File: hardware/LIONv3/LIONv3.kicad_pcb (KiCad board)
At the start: 4 copper layers, 51 x 86 mm, 97 parts, among them SW1 RESET, SW2 BOOT, U1 HC-1_25-2PWT, U10 E80-900M2213S, U11 W25Q16JVSSIQTR, U12 XL-1608UBC-04, U13 XL-1608UGC-04, U14 TPS259474ARPWR, U15 TLV76733DRVR, U16 XL-1608SURC-06, U17 INA226AIDGSR, U18 HC-1_25-2PWT, U19 HC-1_25-2PWT, U2 HC-1_25-2PWT, U20 HC-1_25-2PWT, U21 TCAN3414DR, U3 ESP32-C6-MINI-1-N4, U5 HC-1_25-2PWT, U6 TMP112AIDRLR, U7 USBLC6-2SC6, U8 TYPE-C_16PIN_2MD(073), U9 INA226AIDGSR

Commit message: refactor(hardware): improve via fencing
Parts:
- H1, H2, H3: footprint MountingHole:MountingHole_2.5mm_Pad -> MountingHole:MountingHole_2.5mm
- moved H2 45.3 mm to (71.3, 114.4)
- moved H3 44.5 mm to (116.0, 114.4)
- moved U20 1.61 mm to (110.2, 80.7)
- moved H1 0.92 mm to (116.0, 79.8)
- moved U3 0.22 mm to (82.7, 87.6)
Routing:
- net GND: track 0.00 -> 8.72 mm, vias 296 -> 326
- added copper zone on B.Cu, net GND
- added copper zone on In1.Cu, net GND
- added copper zone on In2.Cu, net GND
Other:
- board size 51 x 86 mm -> 50.2 x 85.2 mm

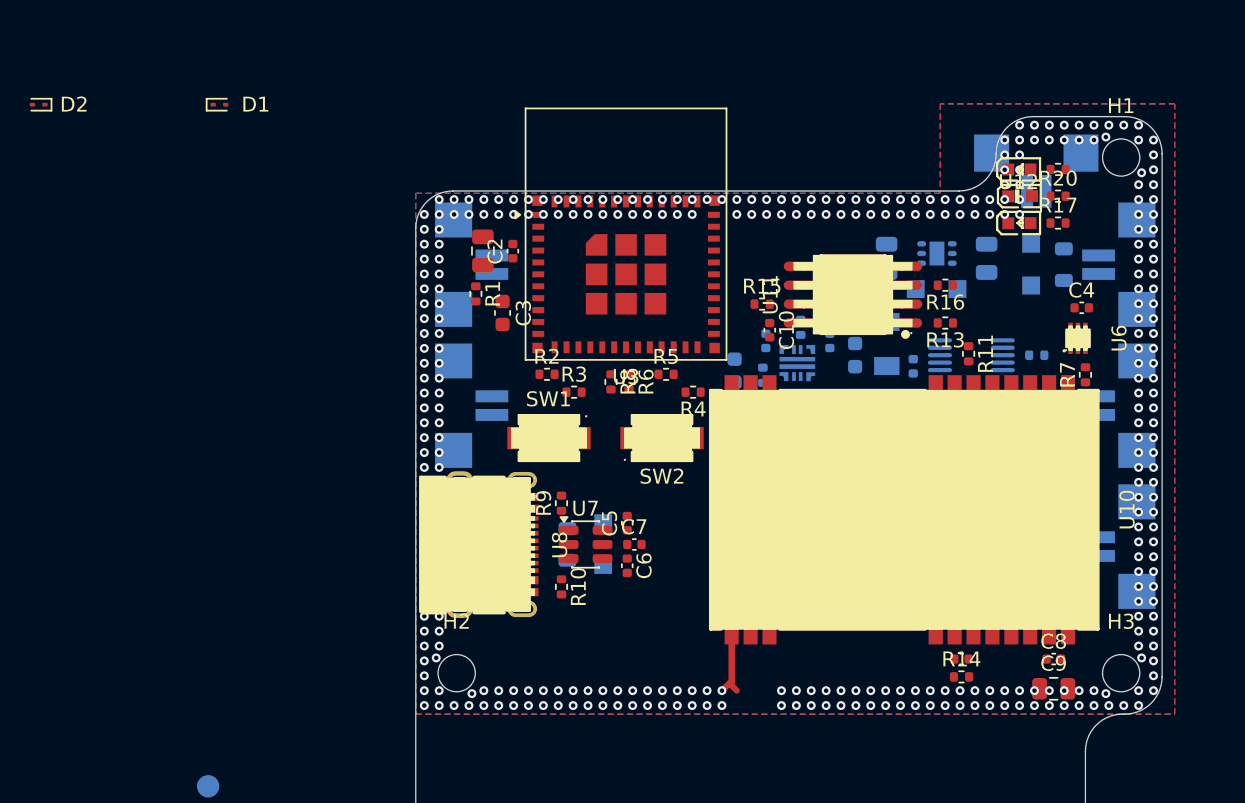
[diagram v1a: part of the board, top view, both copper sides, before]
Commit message: feat(hardware): add LED layout
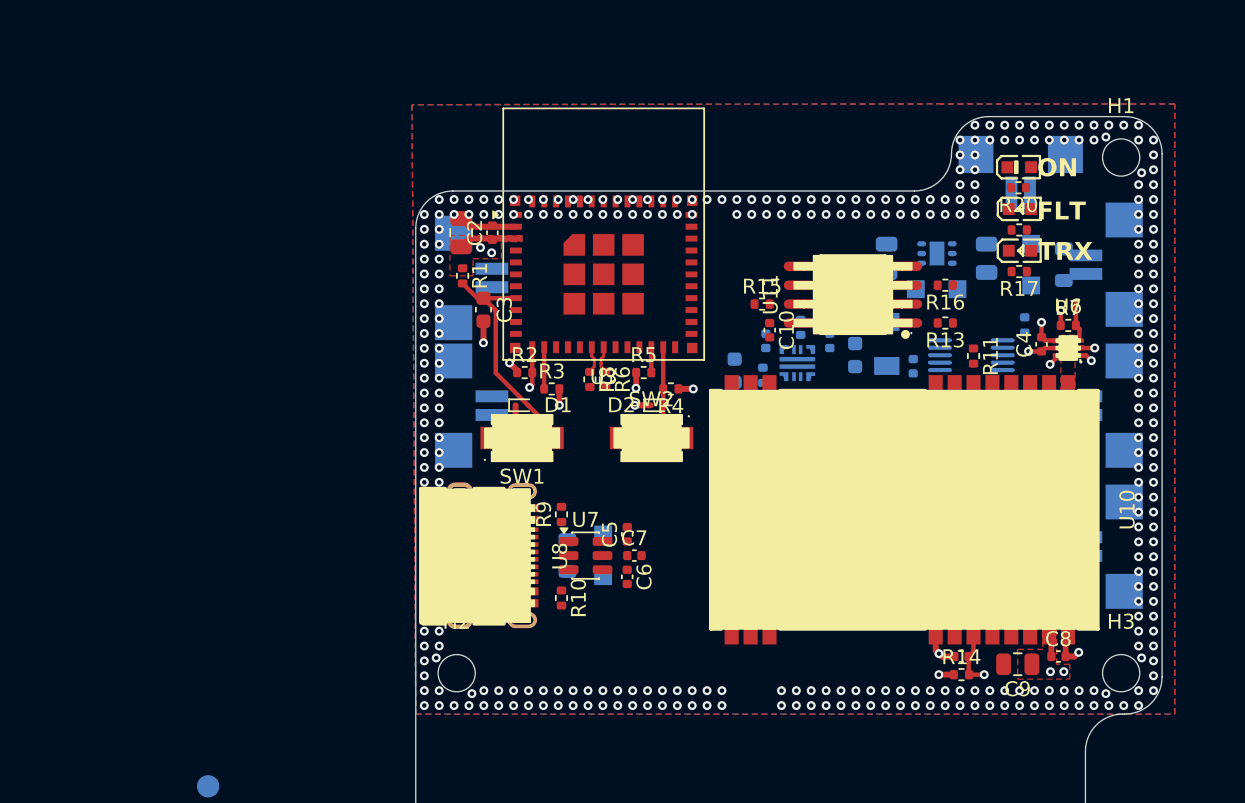
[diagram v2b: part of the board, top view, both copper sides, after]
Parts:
- moved D2 46.2 mm to (84.8, 96.4), turned to 0 degrees
- moved D1 28.7 mm to (75.7, 96.4)
- moved R24 4.83 mm to (109.1, 84.6), turned to 180 degrees
- moved R17 4.18 mm to (109.1, 87.4), turned to 180 degrees
- moved C4 3.65 mm to (110.6, 92.3), turned to 90 degrees
- moved R7 3.51 mm to (112.4, 91.0), turned to 0 degrees
- moved C9 2.93 mm to (109.0, 113.8), turned to 180 degrees
- moved R20 2.72 mm to (109.1, 81.8), turned to 180 degrees
- moved U16 2.65 mm to (109.2, 83.2)
- moved R27 2.19 mm to (109.5, 91.0), turned to 90 degrees
- moved U13 1.95 mm to (109.1, 80.4)
- moved C1 1.91 mm to (71.6, 84.8)
- moved U12 1.86 mm to (109.1, 86.0)
- moved C2 1.85 mm to (73.7, 84.8)
- moved SW1 1.80 mm to (75.7, 98.6), turned to 0 degrees
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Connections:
- net Net-(U3-IO12) renamed /ESP_USB_D-
- net Net-(U3-IO13) renamed /ESP_USB_D+
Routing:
- net Net-(D1-A2): track 0.00 -> 15.4 mm
- net +3.3V: track 0.00 -> 11.0 mm, vias 0 -> 8
- net GND: track 8.72 -> 19.6 mm, vias 326 -> 335
- net /IO9: track 0.00 -> 6.78 mm
- net /LR_RST: track 0.00 -> 4.25 mm, vias 0 -> 1
- net /I2C_SCL: track 0.00 -> 3.74 mm, vias 0 -> 1
- net /I2C_SDA: track 0.00 -> 3.57 mm, vias 0 -> 2
- net 3.3V_RF: track 0.00 -> 2.93 mm, vias 0 -> 3
- net /TMP_ALERT: track 0.00 -> 2.57 mm
- net /ESP_USB_D-: track 0.00 -> 1.85 mm
- net /ESP_USB_D+: track 0.00 -> 1.85 mm
- net /IO8: track 0.00 -> 1.70 mm
- added copper zone on F.Cu, net +3.3V
- added copper zone on F.Cu, net 3.3V_RF
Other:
- outline, holes or cut-outs redrawn
- board text added: "FLT"
- board text added: "ON"
- board text added: "TRX"

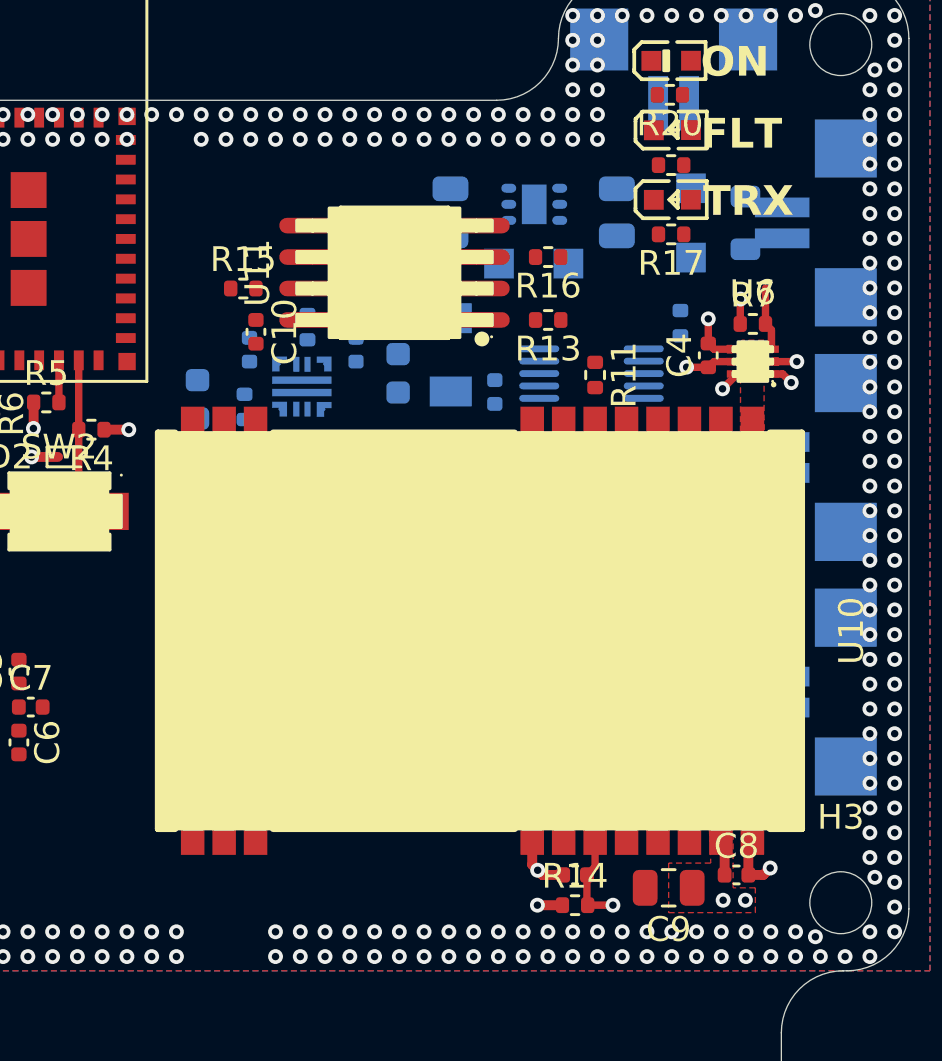
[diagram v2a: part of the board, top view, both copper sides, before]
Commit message: feat(hardware): start PDN design
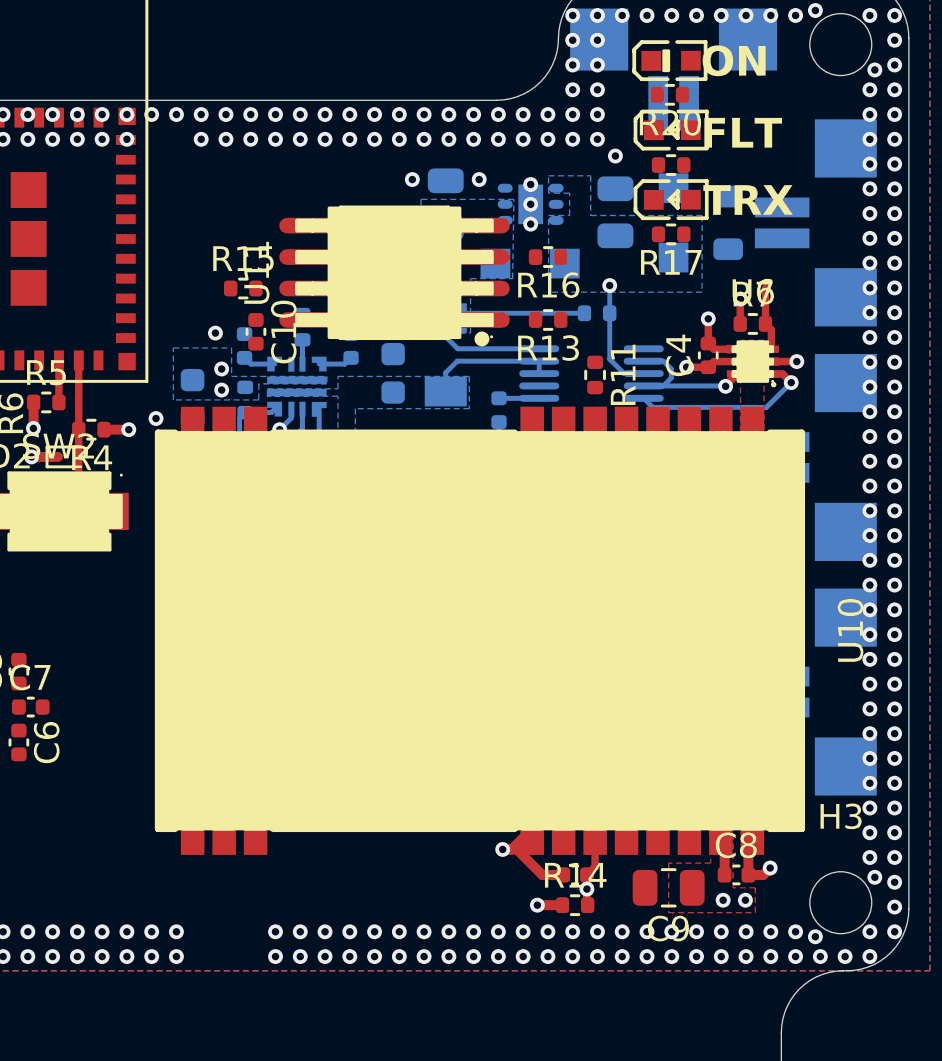
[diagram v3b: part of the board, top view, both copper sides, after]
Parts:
- moved R27 3.39 mm to (106.1, 90.6), turned to 180 degrees
- moved R12 0.88 mm to (99.2, 98.9)
- moved C19 0.75 mm to (102.2, 94.5), turned to -90 degrees
- moved D5 0.70 mm to (109.2, 87.0), turned to 90 degrees
- moved FB2 0.70 mm to (111.4, 87.0), turned to -90 degrees
- moved C16 0.37 mm to (100.0, 86.2)
- moved R19 0.28 mm to (91.9, 94.1)
- moved C17 0.25 mm to (96.2, 91.9)
- moved C18 0.25 mm to (91.9, 91.9)
- moved C14 0.20 mm to (97.9, 93.0)
- moved R21 0.20 mm to (94.9, 97.2)
- moved R22 0.20 mm to (91.7, 96.7)
- moved R26 0.20 mm to (100.0, 92.3)
- moved U14 0.20 mm to (94.0, 93.6)
- moved C13 0.20 mm to (89.8, 94.1)
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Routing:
- net +3.3V: track 11.0 -> 23.7 mm, vias 8 -> 11
- net +3.3V_LDO: track 0.00 -> 12.0 mm
- net GND: track 19.6 -> 30.4 mm, vias 335 -> 348
- net /I2C_SCL: track 3.74 -> 10.3 mm
- net /I2C_SDA: track 3.57 -> 9.58 mm
- net 3.3V_RF: track 2.93 -> 8.43 mm
- net +3.3V_eFuse: track 0.00 -> 5.22 mm
- net /INA_ALERT: track 0.00 -> 4.59 mm, vias 0 -> 1
- net Net-(U14-OVLO/OVCSEL): track 0.00 -> 3.56 mm
- net Net-(U14-EN/UVLO): track 0.00 -> 2.90 mm
- net Net-(U14-FLT#/PGTH): track 0.00 -> 2.89 mm
- net Net-(U14-ITIMER): track 0.00 -> 1.39 mm
- net Net-(U14-DVDT): track 0.00 -> 1.32 mm
- net /POWER/LED_FAULT: track 0.00 -> 1.02 mm, vias 0 -> 1
- net Net-(U14-ILM): track 0.00 -> 0.99 mm
- added copper zone on B.Cu, net +3.3V
- added copper zone on In2.Cu, net +3.3V
- added copper zone on B.Cu, net +3.3V_LDO
- added copper zone on B.Cu, net +3.3V_eFuse
- added copper zone on B.Cu, net +4.69V
- added copper zone on In2.Cu, net 3.3V_RF

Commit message: feat(hardware): improve PCB layout
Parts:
- C12, R11, R14, R15: moved to B.Cu
- C20, C21, C22, D6, JP1, R28, R29, TP1, TP2, TP3, TP4, TP5, TP6, TP7, TP8, TP9, U21: moved to F.Cu
- moved TP10 318.9 mm to (463.3, 86.7)
- moved TP12 318.9 mm to (463.3, 93.8)
- moved H2 295.2 mm to (365.9, 94.9)
- moved TP11 287.0 mm to (423.8, 93.5), turned to 180 degrees
- moved C13 259.0 mm to (348.7, 89.9)
- moved C11 258.1 mm to (359.6, 83.5)
- moved R12 257.6 mm to (356.5, 86.3), turned to 0 degrees
- moved R22 255.9 mm to (347.3, 86.1), turned to 90 degrees
- moved R15 255.7 mm to (346.4, 66.0)
- moved U20 255.6 mm to (364.8, 77.0), turned to -90 degrees
- moved R19 255.5 mm to (347.3, 88.2), turned to 90 degrees
- moved C18 255.4 mm to (347.3, 90.8), turned to -90 degrees
- moved C4 254.2 mm to (364.1, 73.7), turned to -90 degrees
- moved C10 253.7 mm to (344.7, 65.5), turned to 90 degrees
- moved R23 252.6 mm to (345.7, 86.1), turned to 90 degrees
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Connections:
- TP6 pad 1: /SPI_SCK -> /LR_LED
- U3 pad 15: /SPI_SCK -> /LR_LED
- U3 pad 16: /SPI_PICO -> /TMP_ALERT
- U3 pad 19: /LR_LED -> /CAN_RX
- U3 pad 20: /TMP_ALERT -> /CAN_TX
- U3 pad 24: /LR_CS# -> /CAN_STB
- U3 pad 26: /LR_BUSY -> /LR_IRQ
- U3 pad 27: /CAN_STB -> /LR_BUSY
- U3 pad 28: /CAN_TX -> /LR_CS#
- U3 pad 29: /CAN_RX -> /SPI_SCK
- U3 pad 30: /UART_RX -> /SPI_PICO
- U3 pad 31: /UART_TX -> /SPI_POCI
- U3 pad 5: /SPI_POCI -> /UART_RX
- U3 pad 6: /LR_IRQ -> /UART_TX
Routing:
- net /SPI_POCI: track 0.00 -> 34.7 mm, vias 0 -> 2
- net /LR_IRQ: track 0.00 -> 32.3 mm
- net /SPI_PICO: track 0.00 -> 29.6 mm, vias 0 -> 2
- net /SPI_SCK: track 0.00 -> 29.1 mm, vias 0 -> 2
- net /LR_RST: track 3.85 -> 30.8 mm, vias 1 -> 2
- net /LR_CS#: track 0.00 -> 23.4 mm, vias 0 -> 1
- net /LR_BUSY: track 0.00 -> 21.8 mm
- net +3.3V: track 23.7 -> 9.17 mm, vias 11 -> 24
- net /TMP_ALERT: track 2.57 -> 14.1 mm, vias 0 -> 1
- net GND: track 30.4 -> 18.9 mm, vias 348 -> 368
- net Net-(D1-A2): track 15.4 -> 7.49 mm
- net /I2C_SDA: track 9.58 -> 15.4 mm, vias 2 -> 1
- net +3.3V_LDO: track 12.0 -> 7.87 mm, vias 0 -> 2
- net /IO9: track 6.78 -> 3.84 mm
- net Net-(FB1-Pad2): track 0.00 -> 2.50 mm, vias 0 -> 2
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- added copper zone on B.Cu, net 3.3V_RF
- added copper zone on B.Cu, net Net-(D3-A)
- added copper zone on B.Cu, net Net-(FB1-Pad2)
- removed copper zone on F.Cu, net GND
- removed copper zone on In1.Cu, net GND
- removed copper zone on In2.Cu, net GND
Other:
- board size 50.2 x 85.2 mm -> 50.1 x 85.2 mm

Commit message: feat(hardware): finish PDN
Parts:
- removed C20: 10uF, Capacitor_SMD:C_0805_2012Metric
- removed C21: 100nF, Capacitor_SMD:C_0402_1005Metric
- removed C22: 4.7nF, Capacitor_SMD:C_0402_1005Metric
- removed D6: TI ESD752DBZR, Package_TO_SOT_SMD:SOT-23-3
- removed JP1: SolderJumper_3_Open, Jumper:SolderJumper-3_P2.0mm_Open_TrianglePad1.0x1.5mm
- removed R28, R29: 59, Resistor_SMD:R_0402_1005Metric
- removed TP1, TP10, TP11, TP12, TP2, TP3, TP4, TP5, TP6, TP7, TP8, TP9: TestPoint_Square, TestPoint:TestPoint_Pad_D1.5mm
- removed U21: TCAN3414DR, LIONv3-Footprints:SOIC-8_L4.9-W3.9-P1.27-LS6.0-BL
- R10, R9: moved to B.Cu
- moved U7 114.9 mm to (330.1, 86.8)
- moved U5 43.3 mm to (364.8, 68.2), turned to -90 degrees
- moved R5 41.1 mm to (333.2, 75.2), turned to 90 degrees
- moved U18 39.9 mm to (322.3, 76.6), turned to 90 degrees
- moved FB2 38.1 mm to (325.9, 77.6)
- moved C5 37.6 mm to (333.9, 88.2), turned to -90 degrees
- moved C7 36.7 mm to (334.3, 86.8)
- moved C6 36.4 mm to (333.9, 85.3), turned to 90 degrees
- moved R6 35.0 mm to (330.2, 75.2), turned to -90 degrees
- moved R3 34.3 mm to (326.7, 74.8)
- moved R8 33.9 mm to (329.2, 75.2), turned to -90 degrees
- moved D5 33.4 mm to (328.1, 79.5), turned to 90 degrees
- moved R2 32.3 mm to (324.7, 74.8)
- moved R10 29.6 mm to (323.5, 89.0), turned to 180 degrees
- moved R9 29.3 mm to (323.5, 86.0), turned to 180 degrees
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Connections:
- U7 pad 1: /D+ -> /D-
- U7 pad 3: /D- -> /D+
- U7 pad 4: /USB_D- -> /USB_D+
- U7 pad 6: /USB_D+ -> /USB_D-
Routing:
- net /INA_ALERT: track 3.71 -> 32.9 mm, vias 0 -> 3
- net /USB_D+: track 0.00 -> 27.3 mm
- net /USB_D-: track 0.00 -> 26.6 mm
- net /I2C_SCL: track 11.7 -> 25.8 mm, vias 1 -> 4
- net /I2C_SDA: track 15.4 -> 26.6 mm, vias 1 -> 2
- net GND: track 18.9 -> 10.1 mm, vias 368 -> 375
- net Net-(D1-A2): track 7.49 -> 14.0 mm
- net +3.3V: track 9.17 -> 14.2 mm, vias 24 -> 29
- net /IO9: track 3.84 -> 7.55 mm
- net /D-: track 0.00 -> 3.39 mm
- net /D+: track 0.00 -> 3.39 mm
- net +4.69V: track 0.00 -> 2.55 mm
- net /ESP_USB_D-: track 0.00 -> 1.90 mm
- net /ESP_USB_D+: track 0.00 -> 1.90 mm
- net Net-(U8-CC2): track 0.00 -> 1.89 mm, vias 0 -> 1
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- added copper zone on F.Cu, net GND
- added copper zone on In1.Cu, net GND
- added copper zone on In2.Cu, net GND
- added copper zone on B.Cu, net Net-(D5-A)
- added copper zone on B.Cu, net Net-(FB2-Pad2)
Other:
- board text added: "BOOT"
- board text added: "C6"
- board text added: "EN"
- board text added: "FLASH"
- board text added: "LIONv3-R"

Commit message: feat(hardware): route USB-C and CANbus differential pairs
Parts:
- added C20: 10uF, Capacitor_SMD:C_0805_2012Metric, F.Cu at (373.1, 53.8)
- added C21: 100nF, Capacitor_SMD:C_0402_1005Metric, F.Cu at (370.8, 65.2)
- added C22: 4.7nF, Capacitor_SMD:C_0402_1005Metric, F.Cu at (360.1, 60.7)
- added D6: TI ESD752DBZR, Package_TO_SOT_SMD:SOT-23-3, B.Cu at (360.1, 67.1)
- added JP1: SolderJumper_3_Open, Jumper:SolderJumper-3_P2.0mm_Open_TrianglePad1.0x1.5mm, F.Cu at (360.1, 63.0)
- added R28: 59, Resistor_SMD:R_0402_1005Metric, B.Cu at (361.2, 64.5)
- added R29: 59, Resistor_SMD:R_0402_1005Metric, B.Cu at (359.0, 64.5)
- added U21: TCAN3414DR, LIONv3-Footprints:SOIC-8_L4.9-W3.9-P1.27-LS6.0-BL, B.Cu at (354.3, 70.7)
- moved R17 15.8 mm to (375.7, 68.2)
- moved R20 15.8 mm to (375.7, 62.2)
- moved R24 15.8 mm to (375.7, 65.2)
- moved U13 15.8 mm to (375.4, 63.7)
- moved U12 15.8 mm to (375.5, 69.7)
- moved U16 15.8 mm to (375.5, 66.7)
- moved C7 7.37 mm to (329.7, 81.0), turned to 90 degrees
- moved C5 7.29 mm to (331.1, 81.5), turned to 0 degrees
- moved C6 6.82 mm to (328.3, 81.5), turned to 180 degrees
- moved U7 2.75 mm to (329.7, 84.1), turned to 90 degrees
- moved FB1 1.54 mm to (328.9, 87.3)
- moved D3 1.20 mm to (331.1, 87.0)
- moved U19 0.72 mm to (364.8, 76.3)
- moved C15 0.50 mm to (331.5, 91.3)
- moved U5 0.50 mm to (364.8, 67.7)
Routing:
- net /USB_D+: track 27.3 -> 7.63 mm
- net /USB_D-: track 26.6 -> 7.63 mm
- net /CAN_P: track 0.00 -> 11.9 mm
- net /CAN_N: track 0.00 -> 11.3 mm
- net /I2C_SCL: track 25.8 -> 17.2 mm, vias 4 -> 3
- net /I2C_SDA: track 26.6 -> 19.3 mm, vias 2 -> 1
- net /D+: track 3.39 -> 9.59 mm
- net /D-: track 3.39 -> 8.84 mm
- net Net-(JP1-C): track 0.00 -> 1.85 mm
- net Net-(JP1-B): track 0.00 -> 1.61 mm, vias 0 -> 1
- net Net-(JP1-A): track 0.00 -> 1.61 mm, vias 0 -> 1
- net +4.69V: track 2.55 -> 3.85 mm, vias 0 -> 1
- net GND: track 10.1 -> 11.3 mm, vias 375 -> 381
- net /SPI_SCK: track 29.1 -> 28.1 mm
- net +3.3V_LDO: track 6.03 -> 6.68 mm
